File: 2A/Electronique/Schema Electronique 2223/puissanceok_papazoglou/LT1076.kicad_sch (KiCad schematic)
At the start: 11 parts

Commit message: minimal changes, components
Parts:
- removed C?: 100u, Capacitor_SMD:CP_Elec_6.3x7.7, symbol Device:C_Polarized
- added C301: 100u, Capacitor_SMD:CP_Elec_6.3x7.7, symbol Device:C_Polarized_Small
- C304, C305: MFR 865060240001 -> (none); MPN (none) -> 865060240001
- L?: MFR 7447709220 -> (none); MPN (none) -> 74404084220
- U?: MPN (none) -> LT1076CR
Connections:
- net GND: now also C301.2
- net Vin: now also C301.1
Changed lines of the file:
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@@
-    (stroke (width 0) (type default))
-  )
-  (wire (pts (xy 102.87 68.58) (xy 102.87 69.85))
     (stroke (width 0) (type default))
   )
@@
     (stroke (width 0) (type default))
   )
+  (wire (pts (xy 102.87 68.58) (xy 102.87 71.12))
+    (stroke (width 0) (type default))
+  )
   (wire (pts (xy 148.59 114.3) (xy 148.59 115.57))
     (stroke (width 0) (type default))
@@
     (stroke (width 0) (type default))
   )
-  (wire (pts (xy 102.87 77.47) (xy 102.87 78.74))
+  (wire (pts (xy 102.87 76.2) (xy 102.87 78.74))
     (stroke (width 0) (type default))
   )
@@
     (effects (font (size 1.27 1.27)) (justify right))
   )
-  (symbol (lib_id "Device:C_Polarized") (at 102.87 73.66 0) (unit 1)
-    (in_bom yes) (on_board yes) (dnp no)
-    (property "Reference" "C?" (at 93.98 72.39 0)
-      (effects (font (size 1.27 1.27)) (justify left))
-    )
-    (property "Value" "100u" (at 93.98 74.93 0)
-      (effects (font (size 1.27 1.27)) (justify left))
-    )
-    (property "Footprint" "Capacitor_SMD:CP_Elec_6.3x7.7" (at 103.8352 77.47 0)
-      (effects (font (size 1.27 1.27)) hide)
-    )
-    (property "Datasheet" "https://www.we-online.com/components/products/datasheet/865060445005.pdf" (at 102.87 73.66 0)
-      (effects (font (size 1.27 1.27)) hide)
-    )
-    (property "MPN" "865060445005" (at 102.87 73.66 0)
-      (effects (font (size 1.27 1.27)) hide)
-    )
-    (property "Vmax" "25V" (at 102.87 73.66 0)
-      (effects (font (size 1.27 1.27)) hide)
-    )
-    (pin "1")
-    (pin "2")
-    (instances
-      (project "puissance"
-        (path "/0d130b37-34b7-46a9-87e1-2e8471e42169/1102c957-0c72-4739-9178-7c6acddebd3f"
-          (reference "C?") (unit 1)
-        )
-        (path "/0d130b37-34b7-46a9-87e1-2e8471e42169/fb385e64-ed51-4fb9-92be-be410faa5a42"
-          (reference "C?") (unit 1)
-        )
-      )
-      (project "puissanceok"
-        (path "/50648b18-b1a7-4d76-a5dd-1fad5f3e825e/d0016765-fb7e-4c4e-9d8c-f91c29732bdf"
-          (reference "C301") (unit 1)
-        )
-        (path "/50648b18-b1a7-4d76-a5dd-1fad5f3e825e/7ec9b85e-02d5-4657-bc47-51feb658e8df"
-          (reference "C601") (unit 1)
-        )
-      )
-      (project "LT1076"
-        (path "/7a72ba39-2c16-4369-b19e-b43db5a2fe7b"
-          (reference "C?") (unit 1)
-        )
-      )
-    )
-  )
   (symbol (lib_id "power:PWR_FLAG") (at 157.48 68.58 0) (unit 1)
     (in_bom yes) (on_board yes) (dnp no) (fields_autoplaced)
@@
       (effects (font (size 1.27 1.27)) hide)
     )
-    (property "MFR" "865060240001" (at 171.45 74.93 0)
+    (property "MPN" "865060240001" (at 171.45 74.93 0)
       (effects (font (size 1.27 1.27)) hide)
     )
@@
     )
   )
+  (symbol (lib_id "Device:C_Polarized_Small") (at 102.87 73.66 0) (unit 1)
+    (in_bom yes) (on_board yes) (dnp no)
+    (property "Reference" "C301" (at 105.41 73.66 0)
+      (effects (font (size 1.27 1.27)) (justify left))
+    )
+    (property "Value" "100u" (at 104.14 76.2 0)
+      (effects (font (size 1.27 1.27)) (justify left))
+    )
+    (property "Footprint" "Capacitor_SMD:CP_Elec_6.3x7.7" (at 102.87 73.66 0)
+      (effects (font (size 1.27 1.27)) hide)
+    )
+    (property "Datasheet" "https://www.we-online.com/components/products/datasheet/865060445005.pdf" (at 102.87 73.66 0)
+      (effects (font (size 1.27 1.27)) hide)
+    )
+    (property "MPN" "865060445005" (at 102.87 73.66 0)
+      (effects (font (size 1.27 1.27)) hide)
+    )
+    (property "Vmax" "25V" (at 102.87 73.66 0)
+      (effects (font (size 1.27 1.27)) hide)
+    )
+    (pin "1")
+    (pin "2")
+    (instances
+      (project "puissanceok"
+        (path "/50648b18-b1a7-4d76-a5dd-1fad5f3e825e/d0016765-fb7e-4c4e-9d8c-f91c29732bdf"
+          (reference "C301") (unit 1)
+        )
+        (path "/50648b18-b1a7-4d76-a5dd-1fad5f3e825e/7ec9b85e-02d5-4657-bc47-51feb658e8df"
+          (reference "C601") (unit 1)
+        )
+      )
+    )
+  )
   (symbol (lib_id "Device:R_Small") (at 110.49 87.63 0) (unit 1)
     (in_bom yes) (on_board yes) (dnp no)
@@
       (effects (font (size 1.27 1.27)) hide)
     )
-    (property "MFR" "865060240001" (at 161.29 74.93 0)
+    (property "MPN" "865060240001" (at 161.29 74.93 0)
       (effects (font (size 1.27 1.27)) hide)
     )
@@
     )
     (property "Datasheet" "https://www.mouser.fr/datasheet/2/609/1074fds-3123169.pdf" (at 118.11 72.39 0)
+      (effects (font (size 1.27 1.27)) hide)
+    )
+    (property "MPN" "LT1076CR" (at 123.19 74.93 0)
       (effects (font (size 1.27 1.27)) hide)
     )
@@
       (effects (font (size 1.27 1.27)) hide)
     )
-    (property "MFR" "7447709220" (at 148.59 68.58 90)
-      (effects (font (size 1.27 1.27)) hide)
-    )
+    (property "MPN" "74404084220" (at 148.59 68.58 90)
+      (effects (font (size 1.27 1.27)) hide)
+    )

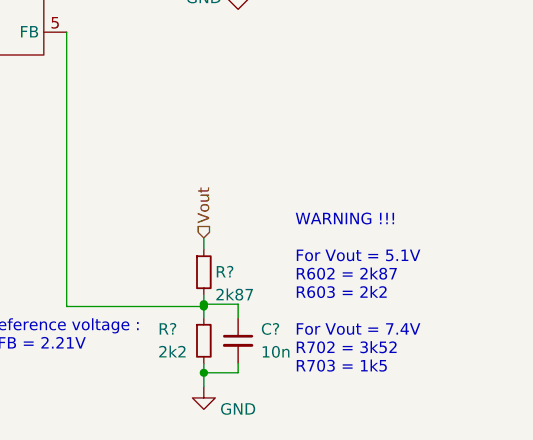
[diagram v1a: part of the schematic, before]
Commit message: modif resistance
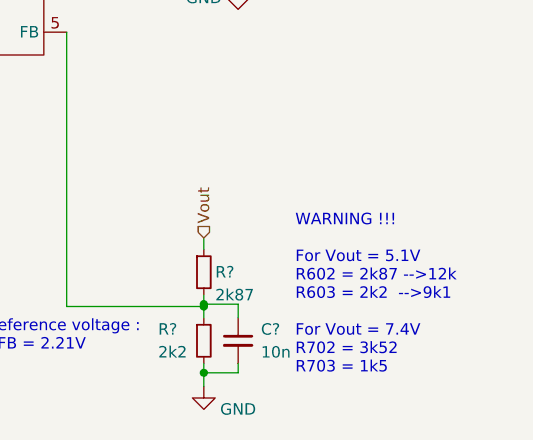
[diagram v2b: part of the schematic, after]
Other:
- note added: "WARNING !!! For Vout = 5.1V R602 = 2k87 -->12k R603 = 2k2 -->9k1 For Vout = 7.4V R702 = 3k52 R703 = 1k5"
- note removed: "WARNING !!! For Vout = 5.1V R602 = 2k87 R603 = 2k2 For Vout = 7.4V R702 = 3k52 R703 = 1k5"
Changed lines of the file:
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@@
     (effects (font (size 1.27 1.27)) (justify left bottom))
   )
-  (text "WARNING !!!\n\nFor Vout = 5.1V\nR602 = 2k87\nR603 = 2k2\n\nFor Vout = 7.4V\nR702 = 3k52\nR703 = 1k5"
+  (text "WARNING !!!\n\nFor Vout = 5.1V\nR602 = 2k87 -->12k\nR603 = 2k2  -->9k1\n\nFor Vout = 7.4V\nR702 = 3k52\nR703 = 1k5"
     (at 158.75 121.92 0)
     (effects (font (size 1.27 1.27)) (justify left bottom))
